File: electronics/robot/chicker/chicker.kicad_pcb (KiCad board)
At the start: 2 copper layers, 100 x 98 mm, 36 parts, among them K1 RELAY_2RT, M1 16mm, M2 16mm, M3 16mm, P1 CONN_01X02, P2 CONN_02X06, P3 CONN_01X02, Q1 Q_NMOS_GSD, Q3 Q_NIGBT_GCE, Q4 Q_NIGBT_GCE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

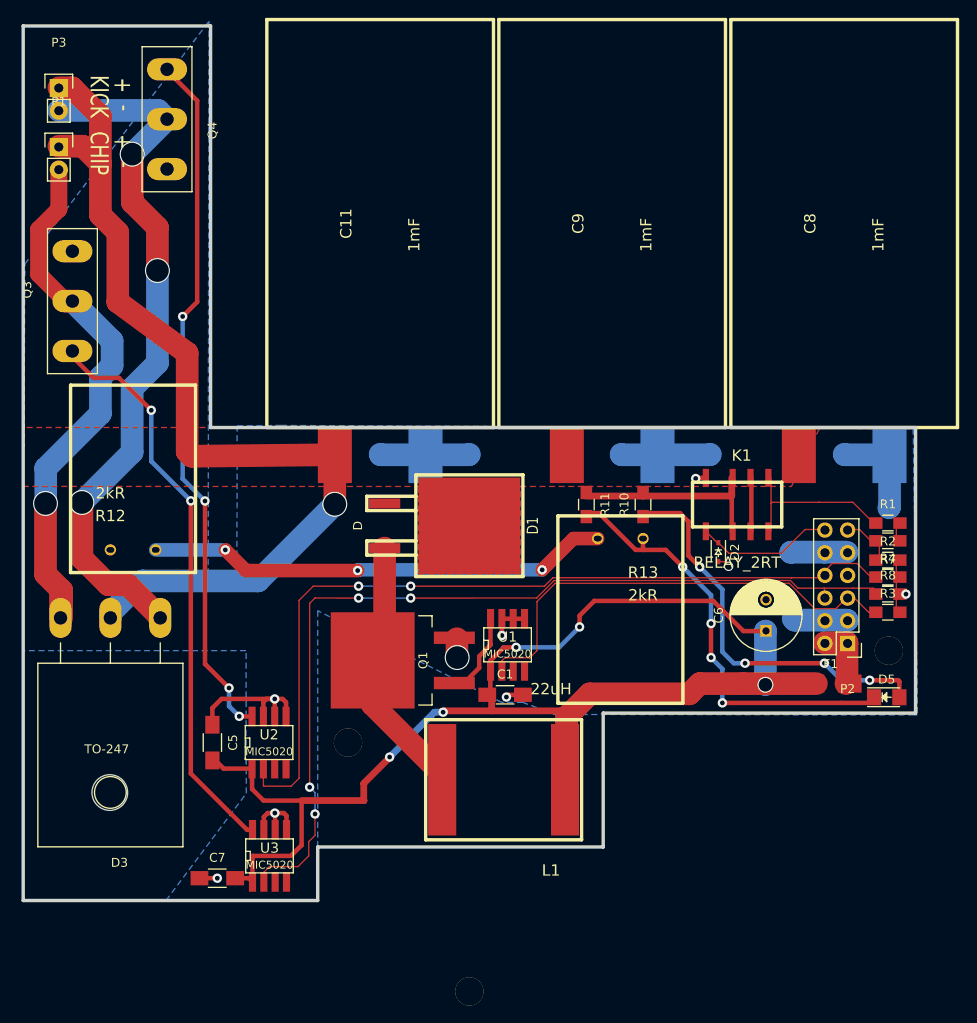
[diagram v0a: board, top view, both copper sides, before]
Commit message: Route high current better and increase clearance.
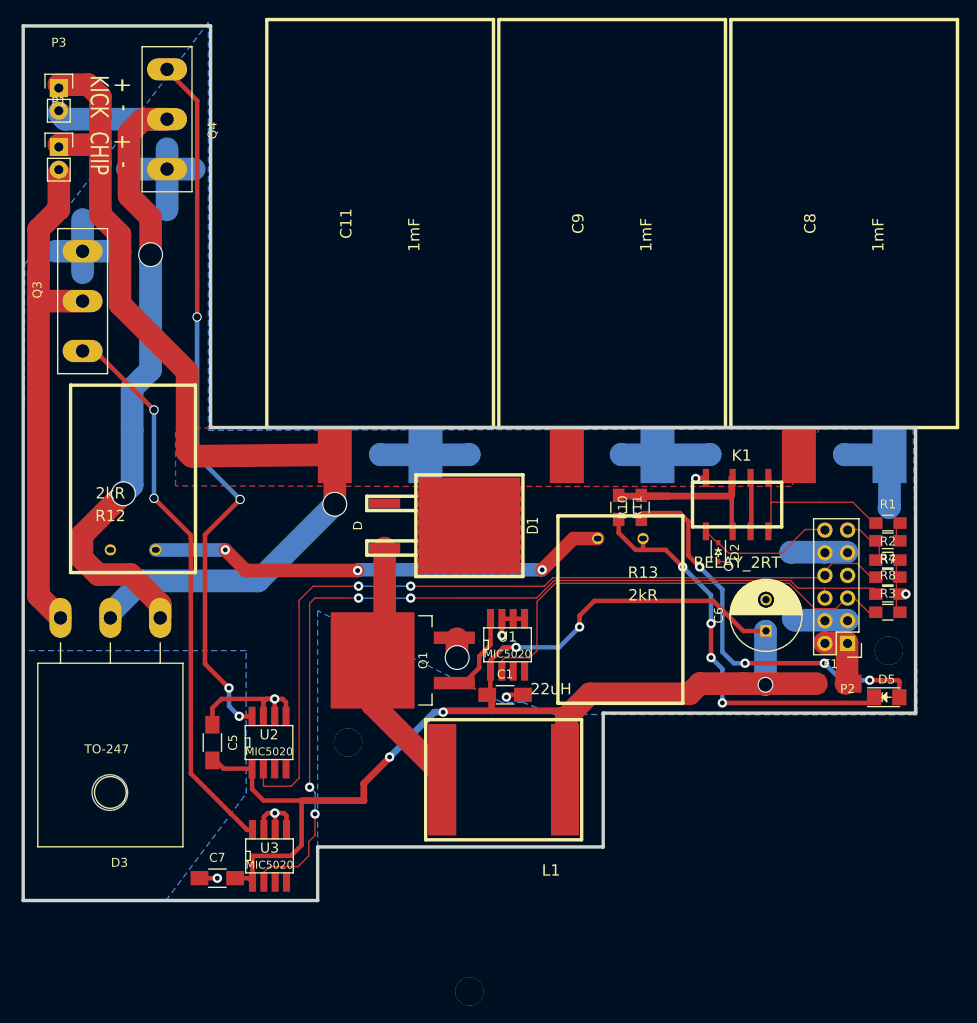
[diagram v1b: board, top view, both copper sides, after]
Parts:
- moved R11 3.63 mm to (121.7, 87.9)
- moved Q3 1.14 mm to (61.7, 64.8)
- moved R10 0.37 mm to (124.3, 87.9)
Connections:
- net Net-(D3-Pad1) renamed /Kick-
- net Net-(D3-Pad3) renamed /Chip-
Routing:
- net GND: track 89.8 -> 117.4 mm
- net /Chip-: track 62.8 -> 56.8 mm, vias 1 -> 0
- net Net-(D5-Pad1): track 49.2 -> 46.1 mm
- net /Kick-: track 79.6 -> 81.6 mm, vias 3 -> 2
- net Net-(Q4-Pad1): track 78.5 -> 80.4 mm
- net Net-(Q3-Pad1): track 64.6 -> 62.7 mm
- net Net-(K1-Pad14): track 22.4 -> 21.6 mm
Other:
- net class HighPower: clearance 0.1524 -> 0.45; trace_width 1.524 -> 2.54; via_dia 1.778 -> 2.794; via_drill 1.524 -> 2.54

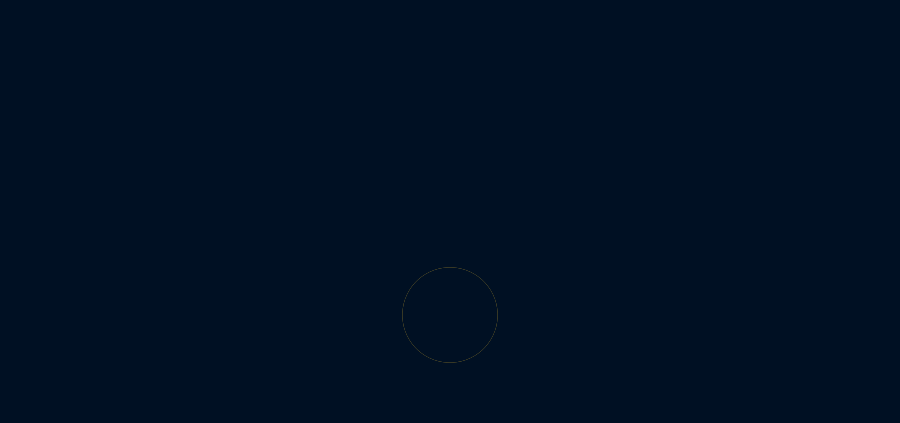
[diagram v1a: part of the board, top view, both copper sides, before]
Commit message: Remove old screw.
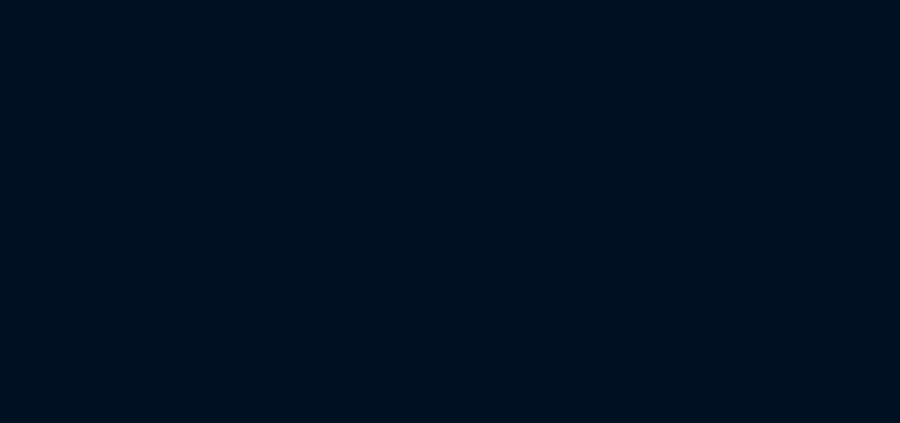
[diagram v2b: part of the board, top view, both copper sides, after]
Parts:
- removed the M1 at (105.0, 142.2)
- renumbered M2 to M1, M3 to M2
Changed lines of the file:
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@@
     (tracks 375)
     (zones 0)
-    (modules 36)
+    (modules 35)
     (nets 28)
   )
@@
     (uvia_drill 0.127)
   )
-  (module thunderbots-modules:M3_MOUNT (layer Front)
-    (at 105.00106 142.191761)
-    (fp_text reference M1 (at 0 -2.54) (layer F.SilkS) hide
-      (effects (font (thickness 0.3048)))
-    )
-    (fp_text value 16mm (at 0 2.54) (layer F.SilkS) hide
-      (effects (font (thickness 0.3048)))
-    )
-    (pad "" thru_hole circle (at 0 0) (size 3.175 3.175) (drill 3.175) (layers *.Cu *.Mask F.SilkS))
-  )
   (module TO_SOT_Packages_THT:TO-247_Horizontal_Neutral123 (layer Front)
     (at 64.77 100.33 180)
@@
   (module thunderbots-modules:M3_MOUNT (layer Front)
     (at 91.39936 114.3)
-    (fp_text reference M2 (at 0 -2.54) (layer F.SilkS) hide
+    (fp_text reference M1 (at 0 -2.54) (layer F.SilkS) hide
       (effects (font (thickness 0.3048)))
     )
@@
   (module thunderbots-modules:M3_MOUNT (layer Front)
     (at 152.00122 104.0003)
-    (fp_text reference M3 (at 0 -2.54) (layer F.SilkS) hide
-      (effects (font (thickness 0.3048)))
-    )
+    (fp_text reference M2 (at 0 -2.54) (layer F.SilkS) hide
+      (effects (font (thickness 0.3048)))
+    )

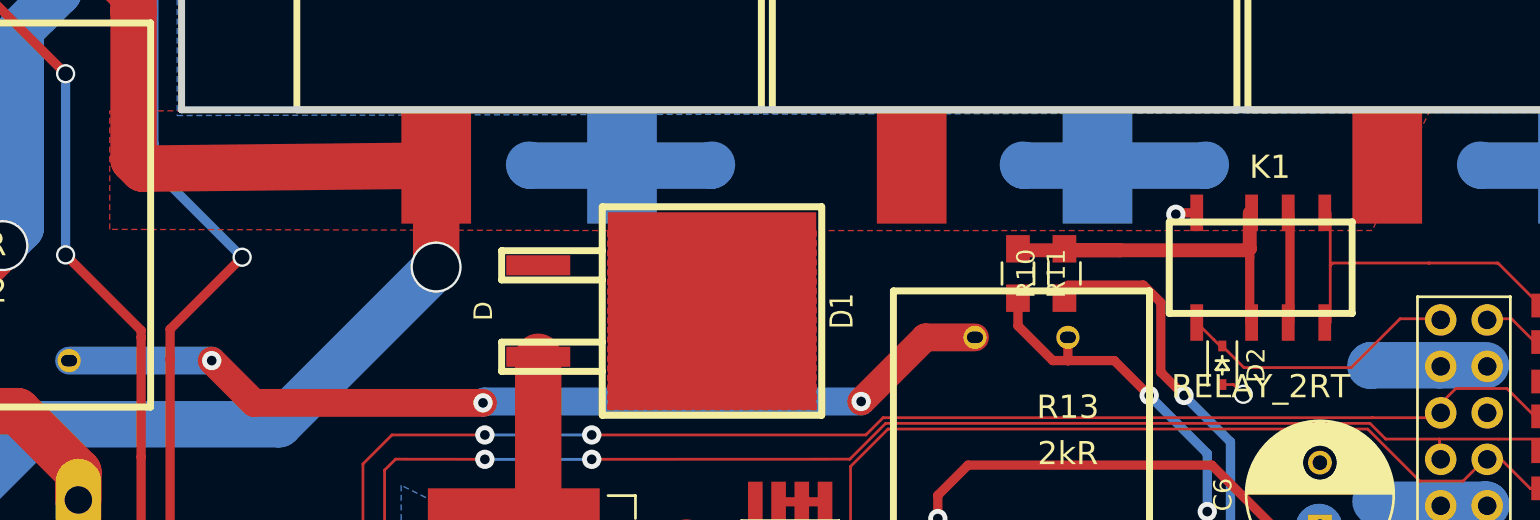
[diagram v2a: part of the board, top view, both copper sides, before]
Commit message: Increase clearance from relay to CAP+.
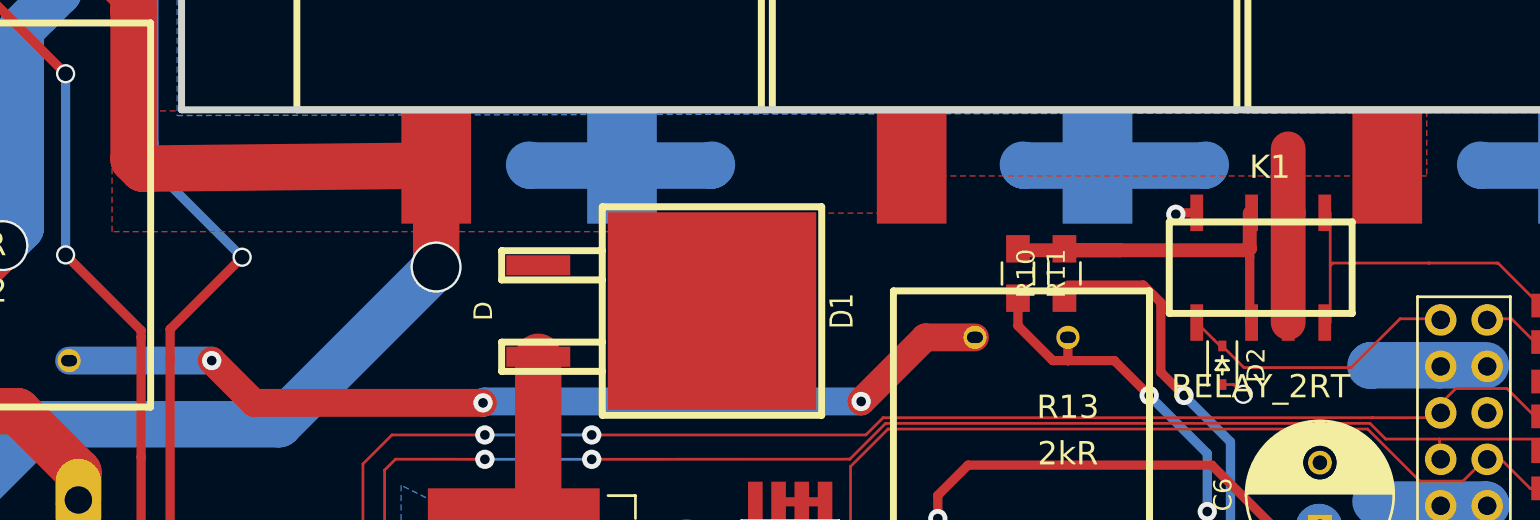
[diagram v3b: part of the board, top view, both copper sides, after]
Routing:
- net /CAP+: track 112.7 -> 116.2 mm
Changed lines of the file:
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@@
     (thickness 1.6002)
     (drawings 82)
-    (tracks 375)
+    (tracks 376)
     (zones 0)
     (modules 35)
@@
   )
   (setup
-    (last_trace_width 2.54)
+    (last_trace_width 1.905)
     (user_trace_width 0.254)
     (user_trace_width 0.508)
@@
   (segment (start 80.645 119.507) (end 80.645 117.221) (width 0.508) (layer Front) (net 1))
   (segment (start 86.19998 120.79986) (end 81.93786 120.79986) (width 0.508) (layer Front) (net 1))
+  (segment (start 136.50468 84.63026) (end 136.50468 90.62974) (width 1.905) (layer Front) (net 2) (status C00000))
+  (segment (start 136.50468 84.63026) (end 136.50468 81.13268) (width 1.905) (layer Front) (net 2))
   (segment (start 63.6524 55.1815) (end 65.8495 57.3786) (width 2.54) (layer Front) (net 2))
   (segment (start 65.8495 65.183407) (end 73.37552 72.709427) (width 2.54) (layer Front) (net 2))
@@
   (segment (start 62.2935 40.5765) (end 58.9915 40.5765) (width 2.54) (layer Front) (net 2))
   (segment (start 63.6524 47.3075) (end 63.6524 44.0944) (width 2.54) (layer Front) (net 2))
-  (segment (start 136.60232 84.63026) (end 136.60232 90.62974) (width 0.508) (layer Front) (net 2))
   (segment (start 64.77 99.78644) (end 68.36664 96.1898) (width 2.54) (layer Back) (net 2))
   (segment (start 68.36664 96.1898) (end 81.32064 96.1898) (width 2.54) (layer Back) (net 2))
@@
     (polygon
       (pts
-        (xy 141.097 85.598) (xy 110.70082 85.60054) (xy 110.70082 95.39986) (xy 99.29876 95.39986) (xy 99.29876 85.60054)
-        (xy 72.0725 85.5345) (xy 72.0725 79.0575) (xy 144.272 78.994)
+        (xy 144.0815 82.6135) (xy 115.8875 82.6135) (xy 115.8875 84.6455) (xy 110.5535 84.6455) (xy 110.5535 95.3135)
+        (xy 99.3775 95.3135) (xy 99.3775 85.6615) (xy 72.1995 85.6615) (xy 72.1995 79.0575) (xy 144.0815 79.0575)
       )
     )

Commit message: updated LED part label
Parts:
- D5: value LED -> RED
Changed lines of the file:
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@@
-(kicad_pcb (version 4) (host pcbnew 4.0.4-stable)
+(kicad_pcb (version 4) (host pcbnew 4.0.2+dfsg1-stable)
   (general
     (links 77)
     (no_connects 0)
-    (area 54.810659 33.808579 155.191461 132.191761)
+    (area 9.421223 13.12164 197.106578 186.575701)
     (thickness 1.6002)
     (drawings 82)
@@
   )
   (setup
-    (last_trace_width 1.905)
+    (last_trace_width 0.1524)
     (user_trace_width 0.254)
     (user_trace_width 0.508)
@@
       (effects (font (size 1 1) (thickness 0.15)))
     )
-    (fp_text value LED (at 0 2) (layer F.Fab)
+    (fp_text value RED (at 0 2) (layer F.Fab)
       (effects (font (size 1 1) (thickness 0.15)))
     )
@@
   (segment (start 80.645 119.507) (end 80.645 117.221) (width 0.508) (layer Front) (net 1))
   (segment (start 86.19998 120.79986) (end 81.93786 120.79986) (width 0.508) (layer Front) (net 1))
-  (segment (start 136.50468 84.63026) (end 136.50468 90.62974) (width 1.905) (layer Front) (net 2) (status C00000))
+  (segment (start 136.50468 84.63026) (end 136.50468 90.62974) (width 1.905) (layer Front) (net 2))
   (segment (start 136.50468 84.63026) (end 136.50468 81.13268) (width 1.905) (layer Front) (net 2))
   (segment (start 63.6524 55.1815) (end 65.8495 57.3786) (width 2.54) (layer Front) (net 2))
